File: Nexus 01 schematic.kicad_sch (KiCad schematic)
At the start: 48 parts, among them J1 Conn_01x02_Male, J2 Conn_01x02_Male, J3 Conn_01x02_Male, J4 Conn_01x02_Male, J5 USB_C_Receptacle_USB2.0, J6 Conn_01x02_Male, Q1 SI2302, Q2 SI2302, Q3 SI2302, Q4 SI2302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

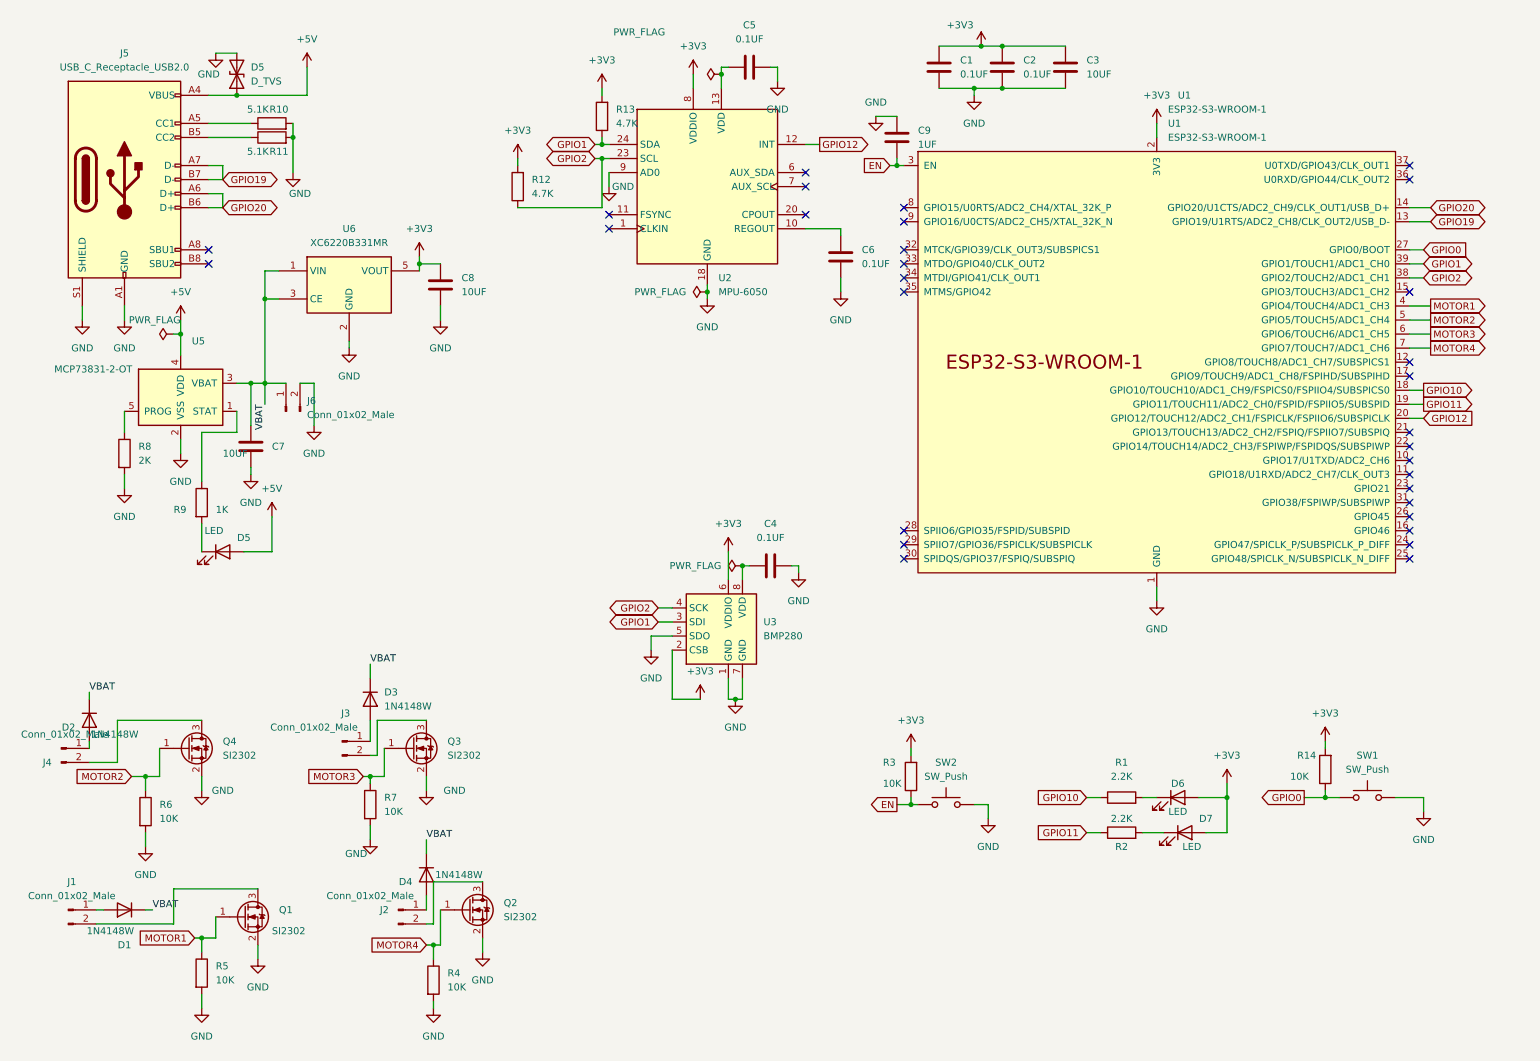
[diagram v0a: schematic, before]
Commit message: Add files via upload
Forgot to change the Diode reference and got a error for duplication updated it
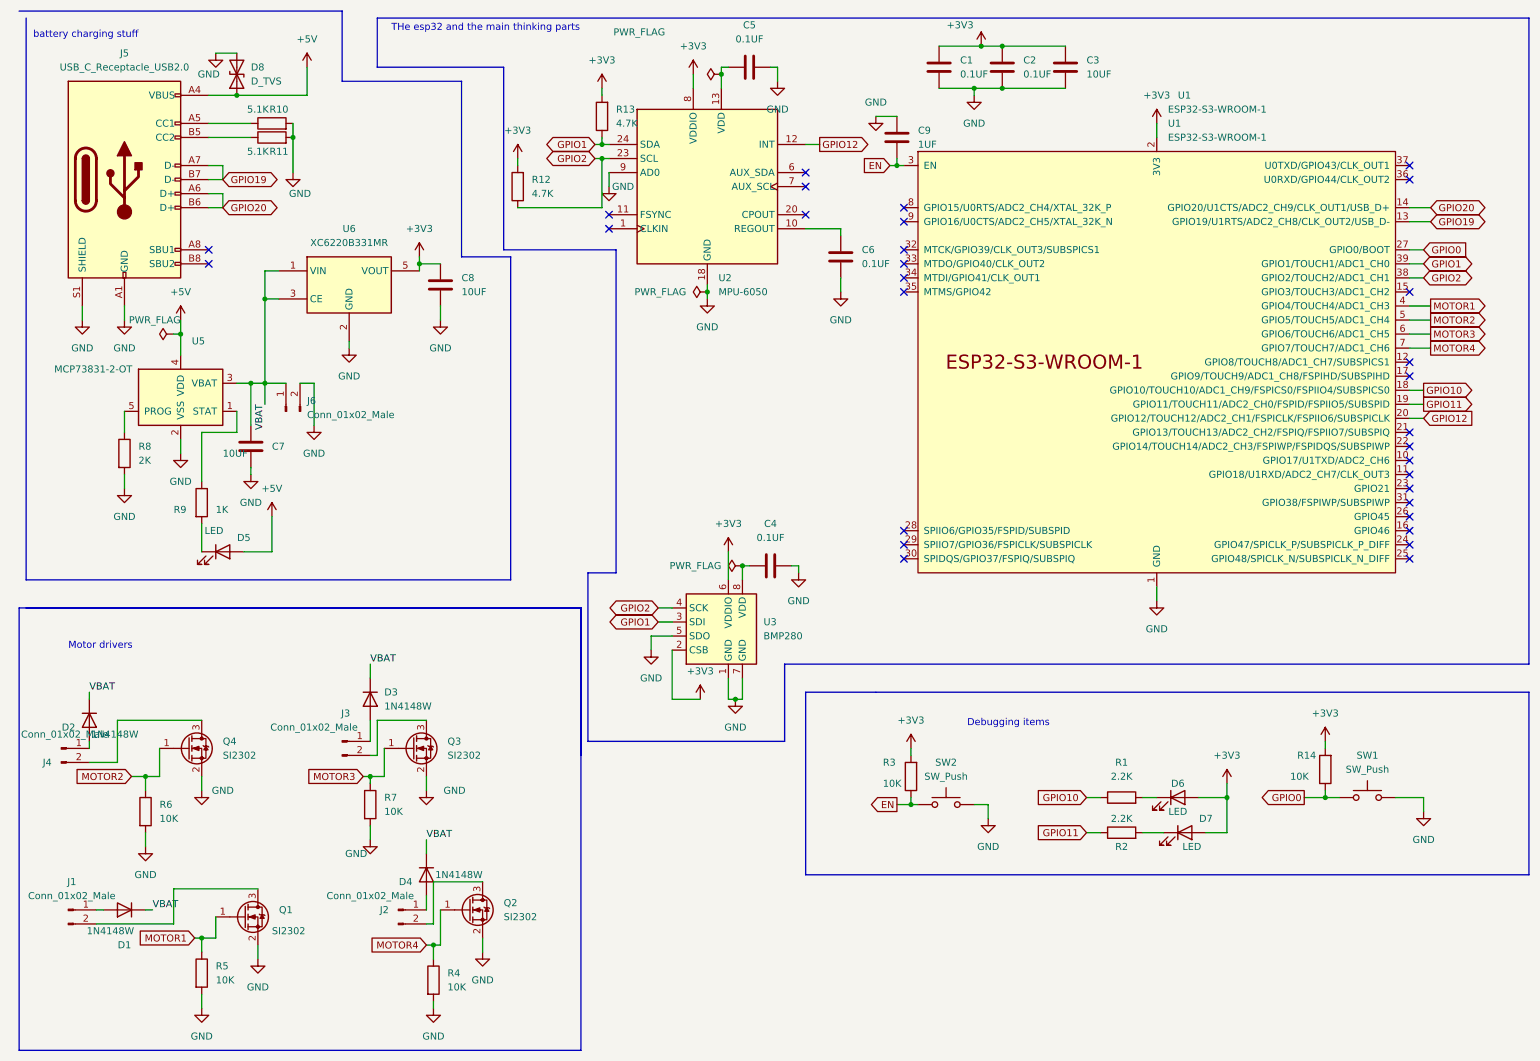
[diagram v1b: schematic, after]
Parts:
- renumbered D5 to D8
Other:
- note added: "Debugging items"
- note added: "Motor drivers"
- note added: "THe esp32 and the main thinking parts"
- note added: "battery charging stuff"
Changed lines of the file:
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@@
+    (stroke (width 0) (type default) (color 0 0 0 0))
+  )
+  (polyline (pts (xy 12.7 12.7) (xy 12.7 114.3))
     (stroke (width 0) (type default) (color 0 0 0 0))
   )
@@
     (stroke (width 0) (type default) (color 0 0 0 0))
   )
+  (polyline (pts (xy 76.2 12.7) (xy 284.48 12.7))
+    (stroke (width 0) (type default) (color 0 0 0 0))
+  )
   (wire (pts (xy 63.5 26.67) (xy 63.5 21.59))
     (stroke (width 0) (type default) (color 0 0 0 0))
@@
     (stroke (width 0) (type default) (color 0 0 0 0))
   )
+  (polyline (pts (xy 113.03 199.39) (xy 11.43 199.39))
+    (stroke (width 0) (type default) (color 0 0 0 0))
+  )
   (wire (pts (xy 85.09 149.86) (xy 85.09 152.4))
     (stroke (width 0) (type default) (color 0 0 0 0))
@@
     (stroke (width 0) (type default) (color 0 0 0 0))
   )
+  (polyline (pts (xy 99.06 54.61) (xy 119.38 54.61))
+    (stroke (width 0) (type default) (color 0 0 0 0))
+  )
   (wire (pts (xy 247.65 153.67) (xy 250.19 153.67))
     (stroke (width 0) (type default) (color 0 0 0 0))
@@
     (stroke (width 0) (type default) (color 0 0 0 0))
   )
+  (polyline (pts (xy 114.3 143.51) (xy 149.86 143.51))
+    (stroke (width 0) (type default) (color 0 0 0 0))
+  )
   (wire (pts (xy 86.36 180.34) (xy 87.63 180.34))
     (stroke (width 0) (type default) (color 0 0 0 0))
@@
     (stroke (width 0) (type default) (color 0 0 0 0))
   )
+  (polyline (pts (xy 119.38 113.03) (xy 114.3 113.03))
+    (stroke (width 0) (type default) (color 0 0 0 0))
+  )
   (wire (pts (xy 57.15 102.87) (xy 57.15 109.22))
     (stroke (width 0) (type default) (color 0 0 0 0))
   )
+  (polyline (pts (xy 153.67 167.64) (xy 284.48 167.64))
+    (stroke (width 0) (type default) (color 0 0 0 0))
+  )
   (wire (pts (xy 36.83 144.78) (xy 36.83 149.86))
     (stroke (width 0) (type default) (color 0 0 0 0))
@@
     (stroke (width 0) (type default) (color 0 0 0 0))
   )
+  (polyline (pts (xy 11.43 119.38) (xy 113.03 119.38))
+    (stroke (width 0) (type default) (color 0 0 0 0))
+  )
+  (polyline (pts (xy 76.2 21.59) (xy 99.06 21.59))
+    (stroke (width 0) (type default) (color 0 0 0 0))
+  )
   (wire (pts (xy 39.37 176.53) (xy 39.37 170.18))
     (stroke (width 0) (type default) (color 0 0 0 0))
   )
+  (polyline (pts (xy 99.06 21.59) (xy 99.06 54.61))
+    (stroke (width 0) (type default) (color 0 0 0 0))
+  )
   (wire (pts (xy 262.89 69.85) (xy 266.7 69.85))
     (stroke (width 0) (type default) (color 0 0 0 0))
@@
     (stroke (width 0) (type default) (color 0 0 0 0))
   )
+  (polyline (pts (xy 12.7 114.3) (xy 100.33 114.3))
+    (stroke (width 0) (type default) (color 0 0 0 0))
+  )
   (wire (pts (xy 189.23 17.78) (xy 200.66 17.78))
     (stroke (width 0) (type default) (color 0 0 0 0))
@@
     (stroke (width 0) (type default) (color 0 0 0 0))
   )
+  (polyline (pts (xy 113.03 119.38) (xy 113.03 199.39))
+    (stroke (width 0) (type default) (color 0 0 0 0))
+  )
   (wire (pts (xy 262.89 46.99) (xy 266.7 46.99))
     (stroke (width 0) (type default) (color 0 0 0 0))
   )
+  (polyline (pts (xy 11.43 199.39) (xy 11.43 119.38))
+    (stroke (width 0) (type default) (color 0 0 0 0))
+  )
   (wire (pts (xy 133.35 22.86) (xy 133.35 25.4))
     (stroke (width 0) (type default) (color 0 0 0 0))
@@
     (stroke (width 0) (type default) (color 0 0 0 0))
   )
+  (polyline (pts (xy 11.43 11.43) (xy 69.85 11.43))
+    (stroke (width 0) (type default) (color 0 0 0 0))
+  )
   (wire (pts (xy 60.96 34.29) (xy 60.96 40.64))
     (stroke (width 0) (type default) (color 0 0 0 0))
@@
     (stroke (width 0) (type default) (color 0 0 0 0))
   )
+  (polyline (pts (xy 91.44 24.13) (xy 69.85 24.13))
+    (stroke (width 0) (type default) (color 0 0 0 0))
+  )
   (wire (pts (xy 77.47 149.86) (xy 77.47 144.78))
     (stroke (width 0) (type default) (color 0 0 0 0))
   )
+  (polyline (pts (xy 149.86 129.54) (xy 284.48 129.54))
+    (stroke (width 0) (type default) (color 0 0 0 0))
+  )
   (wire (pts (xy 60.96 31.75) (xy 60.96 34.29))
     (stroke (width 0) (type default) (color 0 0 0 0))
@@
     (stroke (width 0) (type default) (color 0 0 0 0))
   )
+  (polyline (pts (xy 166.37 134.62) (xy 284.48 134.62))
+    (stroke (width 0) (type default) (color 0 0 0 0))
+  )
   (wire (pts (xy 24.13 143.51) (xy 24.13 144.78))
     (stroke (width 0) (type default) (color 0 0 0 0))
@@
     (stroke (width 0) (type default) (color 0 0 0 0))
   )
+  (polyline (pts (xy 153.67 134.62) (xy 153.67 167.64))
+    (stroke (width 0) (type default) (color 0 0 0 0))
+  )
   (wire (pts (xy 29.21 147.32) (xy 29.21 139.7))
     (stroke (width 0) (type default) (color 0 0 0 0))
   )
+  (polyline (pts (xy 114.3 113.03) (xy 114.3 143.51))
+    (stroke (width 0) (type default) (color 0 0 0 0))
+  )
   (wire (pts (xy 116.84 38.1) (xy 118.11 38.1))
     (stroke (width 0) (type default) (color 0 0 0 0))
@@
     (stroke (width 0) (type default) (color 0 0 0 0))
   )
+  (polyline (pts (xy 69.85 24.13) (xy 69.85 11.43))
+    (stroke (width 0) (type default) (color 0 0 0 0))
+  )
   (wire (pts (xy 153.67 35.56) (xy 156.21 35.56))
     (stroke (width 0) (type default) (color 0 0 0 0))
@@
     (stroke (width 0) (type default) (color 0 0 0 0))
   )
+  (polyline (pts (xy 149.86 143.51) (xy 149.86 129.54))
+    (stroke (width 0) (type default) (color 0 0 0 0))
+  )
   (wire (pts (xy 45.72 26.67) (xy 50.8 26.67))
     (stroke (width 0) (type default) (color 0 0 0 0))
@@
     (stroke (width 0) (type default) (color 0 0 0 0))
   )
+  (polyline (pts (xy 113.03 119.38) (xy 113.03 146.05))
+    (stroke (width 0) (type default) (color 0 0 0 0))
+  )
+  (polyline (pts (xy 119.38 54.61) (xy 119.38 113.03))
+    (stroke (width 0) (type default) (color 0 0 0 0))
+  )
   (wire (pts (xy 160.02 59.69) (xy 160.02 62.23))
     (stroke (width 0) (type default) (color 0 0 0 0))
@@
     (stroke (width 0) (type default) (color 0 0 0 0))
   )
+  (polyline (pts (xy 100.33 55.88) (xy 91.44 55.88))
+    (stroke (width 0) (type default) (color 0 0 0 0))
+  )
+  (polyline (pts (xy 166.37 134.62) (xy 153.67 134.62))
+    (stroke (width 0) (type default) (color 0 0 0 0))
+  )
+  (polyline (pts (xy 91.44 55.88) (xy 91.44 24.13))
+    (stroke (width 0) (type default) (color 0 0 0 0))
+  )
+  (polyline (pts (xy 76.2 12.7) (xy 76.2 21.59))
+    (stroke (width 0) (type default) (color 0 0 0 0))
+  )
+  (polyline (pts (xy 100.33 114.3) (xy 100.33 55.88))
+    (stroke (width 0) (type default) (color 0 0 0 0))
+  )
   (wire (pts (xy 45.72 31.75) (xy 53.34 31.75))
     (stroke (width 0) (type default) (color 0 0 0 0))
@@
     (stroke (width 0) (type default) (color 0 0 0 0))
   )
+  (polyline (pts (xy 284.48 134.62) (xy 284.48 167.64))
+    (stroke (width 0) (type default) (color 0 0 0 0))
+  )
   (wire (pts (xy 83.82 55.88) (xy 83.82 57.15))
     (stroke (width 0) (type default) (color 0 0 0 0))
@@
     (stroke (width 0) (type default) (color 0 0 0 0))
   )
+  (polyline (pts (xy 284.48 129.54) (xy 284.48 12.7))
+    (stroke (width 0) (type default) (color 0 0 0 0))
+  )
   (wire (pts (xy 135.89 62.23) (xy 135.89 63.5))
     (stroke (width 0) (type default) (color 0 0 0 0))
+  )
+  (polyline (pts (xy 12.7 119.38) (xy 113.03 119.38))
+    (stroke (width 0) (type default) (color 0 0 0 0))
+  )
+  (text "THe esp32 and the main thinking parts" (at 78.74 15.24 0)
+    (effects (font (size 1.27 1.27)) (justify left bottom))
+  )
+  (text "Motor drivers" (at 20.32 127 0)
+    (effects (font (size 1.27 1.27)) (justify left bottom))
+  )
+  (text "battery charging stuff" (at 13.97 16.51 0)
+    (effects (font (size 1.27 1.27)) (justify left bottom))
+  )
+  (text "Debugging items" (at 182.88 140.97 0)
+    (effects (font (size 1.27 1.27)) (justify left bottom))
   )
   (label "VBAT" (at 35.56 173.99 0)
@@
   (symbol (lib_id "power:GND") (at 46.99 19.05 0) (unit 1)
     (in_bom yes) (on_board yes)
-    (property "Reference" "#PWR?" (id 0) (at 46.99 25.4 0)
+    (property "Reference" "#PWR0144" (id 0) (at 46.99 25.4 0)
       (effects (font (size 1.27 1.27)) hide)
     )
@@
   (symbol (lib_id "Device:D_TVS") (at 50.8 22.86 90) (unit 1)
     (in_bom yes) (on_board yes) (fields_autoplaced)
-    (property "Reference" "D5" (id 0) (at 53.34 21.5899 90)
+    (property "Reference" "D8" (id 0) (at 53.34 21.5899 90)
       (effects (font (size 1.27 1.27)) (justify right))
     )
@@
     )
     (path "/2920d1a5-7366-42b5-841b-38a89e0ba3de"
-      (reference "#PWR?") (unit 1) (value "GND") (footprint "")
+      (reference "#PWR0144") (unit 1) (value "GND") (footprint "")
     )
     (path "/0471f1c3-4159-4276-b0a5-1d5b9a93f43f"
@@
       (reference "D4") (unit 1) (value "1N4148W") (footprint "Diode_SMD:D_SOD-123")
     )
-    (path "/43fd6388-373b-4f6c-9821-3c57a7a05380"
-      (reference "D5") (unit 1) (value "D_TVS") (footprint "")
-    )
     (path "/ba5e8760-e7ec-4e17-ac4c-6d991664f506"
       (reference "D5") (unit 1) (value "LED") (footprint "")
@@
       (reference "D7") (unit 1) (value "LED") (footprint "")
     )
+    (path "/43fd6388-373b-4f6c-9821-3c57a7a05380"
+      (reference "D8") (unit 1) (value "D_TVS") (footprint "")
+    )
     (path "/02c7c796-d42e-40c8-a708-f50384a7ceb0"
